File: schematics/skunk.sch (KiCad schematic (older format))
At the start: 11 parts

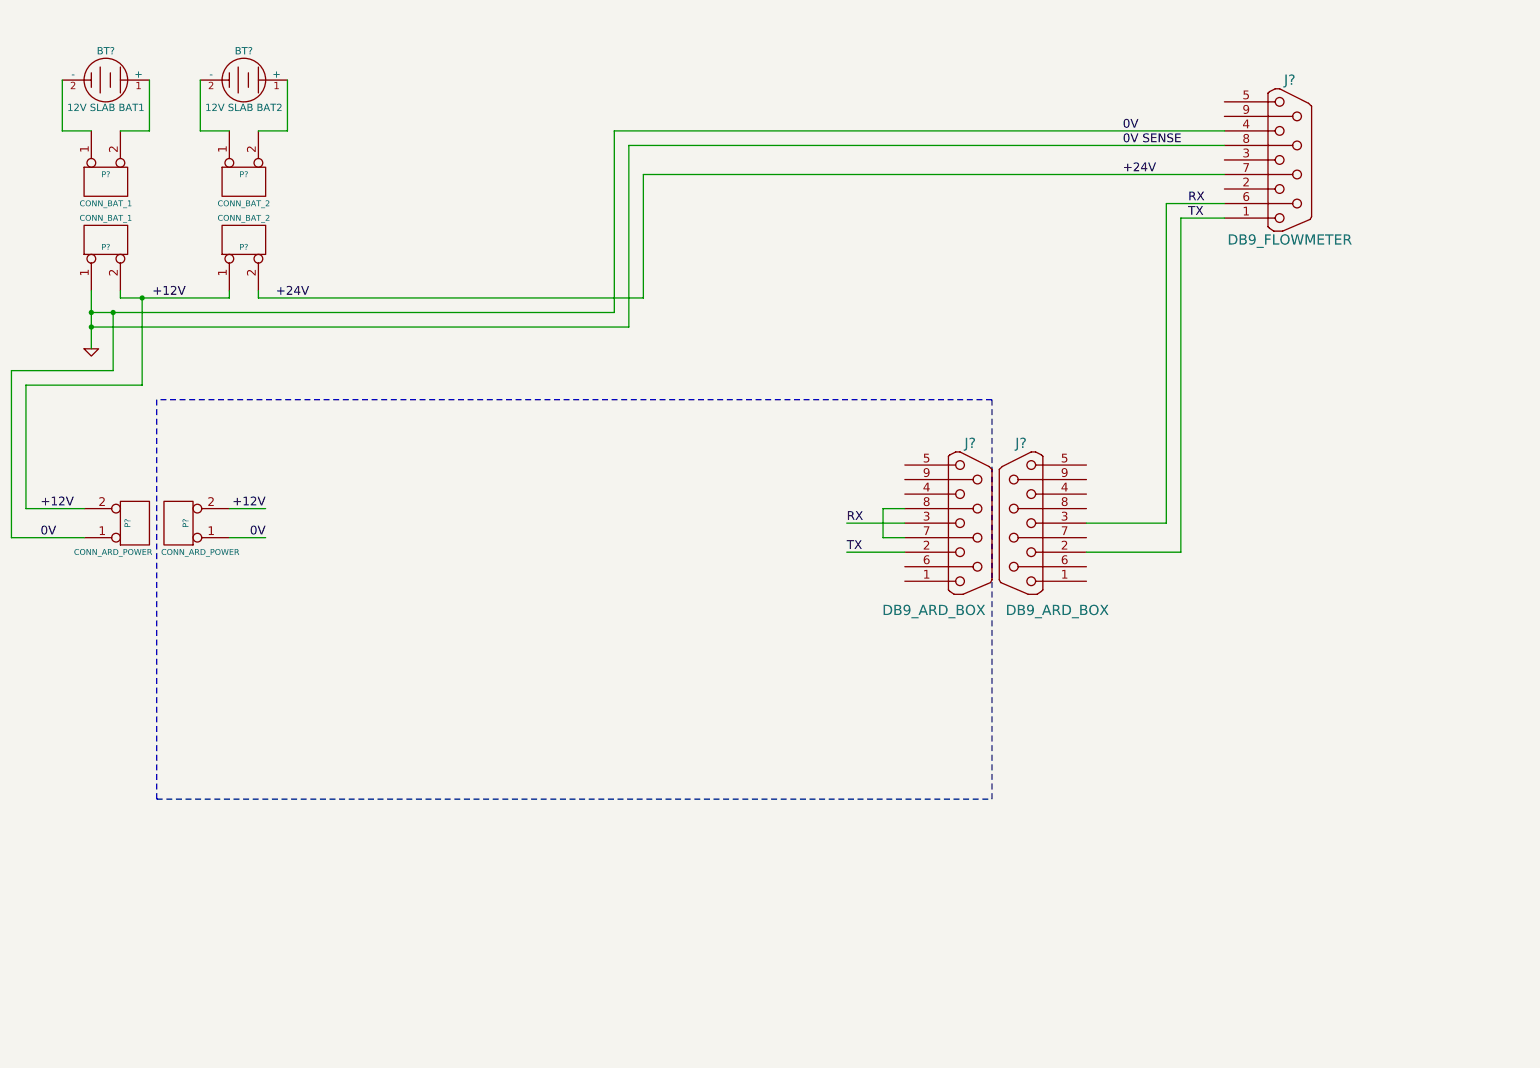
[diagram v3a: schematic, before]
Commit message: Added peripheral DB25 connectors
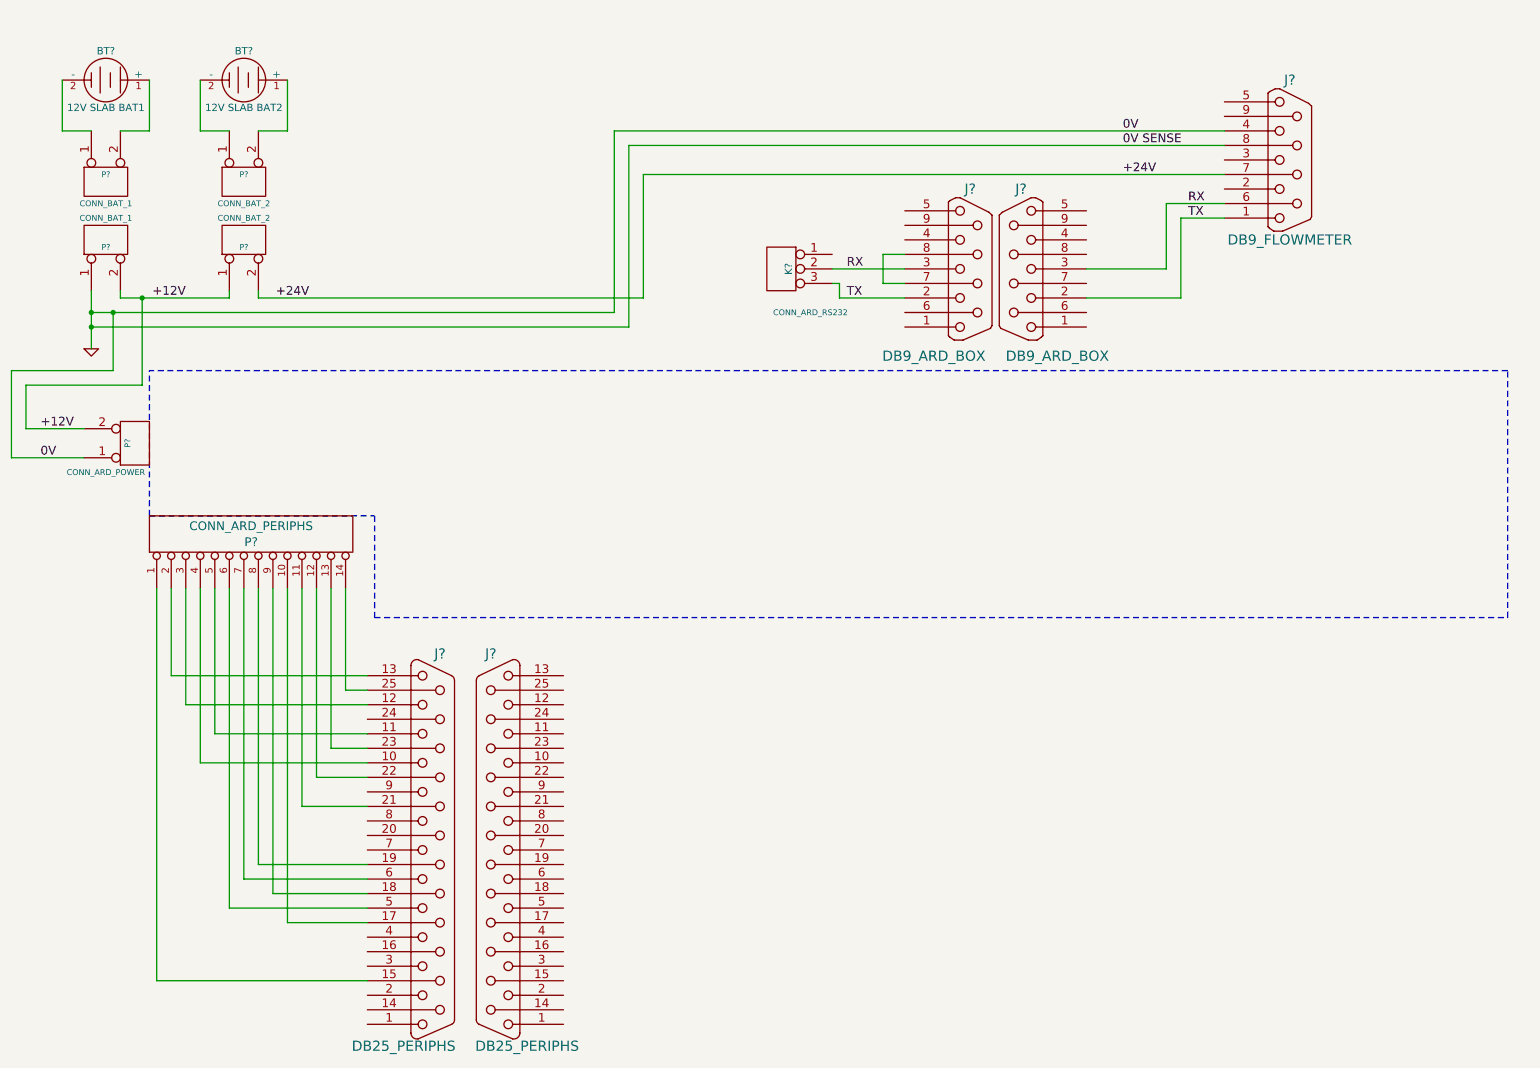
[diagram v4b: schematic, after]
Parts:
- removed P?: CONN_ARD_POWER, symbol CONN_2
- added J? (x2): DB25_PERIPHS, symbol DB25
- added K?: CONN_ARD_RS232, symbol CONN_3
- added P?: CONN_ARD_PERIPHS, symbol CONN_14
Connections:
- net RX: now also K?.2 (PM)
- net TX: now also K?.3 (P3)
- new net: J?.15 (P15), P?.1 (P1)
- new net: J?.17 (P17), P?.10 (P10)
- new net: J?.21 (P21), P?.11 (P11)
- new net: J?.22 (P22), P?.12 (P12)
- new net: J?.23 (P23), P?.13 (P13)
- new net: J?.25 (P25), P?.14 (P14)
- new net: J?.13, P?.2 (P2)
- new net: J?.12, P?.3 (P3)
- new net: J?.10, P?.4 (P4)
- new net: J?.11, P?.5 (P5)
- new net: J?.5, P?.6 (P6)
- new net: J?.6, P?.7 (P7)
- new net: J?.19 (P19), P?.8 (P8)
- new net: J?.18 (P18), P?.9 (P9)
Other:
- moved on the sheet: J?, P?
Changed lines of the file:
@@
-EESchema Schematic File Version 2  date 26/09/2012 21:43:37
+EESchema Schematic File Version 2  date 26/09/2012 22:15:26
 LIBS:power
 LIBS:device
@@
 $EndDescr
 Wire Notes Line
-	1750 5950 1750 3200
-Wire Notes Line
-	1750 5950 7500 5950
-Wire Notes Line
-	7500 5950 7500 3200
-Wire Notes Line
-	7500 3200 1750 3200
+	1700 4000 1700 3000
+Wire Wire Line
+	8150 2500 8800 2500
+Wire Wire Line
+	8800 2500 8800 1950
+Wire Wire Line
+	3200 6700 2250 6700
+Wire Wire Line
+	3200 6500 2350 6500
+Wire Wire Line
+	3200 6000 2750 6000
+Wire Wire Line
+	3200 5700 2050 5700
+Wire Wire Line
+	3200 5500 2150 5500
+Wire Wire Line
+	3200 5200 3050 5200
+Wire Wire Line
+	3200 6800 2650 6800
+Wire Wire Line
+	3050 5200 3050 4500
+Wire Wire Line
+	2850 4500 2850 5800
+Wire Wire Line
+	2650 6800 2650 4500
+Wire Wire Line
+	2450 4500 2450 6400
+Wire Wire Line
+	2250 6700 2250 4500
+Wire Wire Line
+	2050 5700 2050 4500
+Wire Wire Line
+	1850 4500 1850 5100
+Wire Wire Line
+	750  3000 750  3600
 Wire Wire Line
 	9100 1850 8700 1850
 Wire Wire Line
-	8700 1850 8700 4050
-Wire Wire Line
-	6900 4250 6500 4250
-Wire Wire Line
 	9100 1450 5000 1450
 Wire Wire Line
@@
 Wire Wire Line
 	5000 2700 1300 2700
-Wire Wire Line
-	2250 4150 2500 4150
 Connection ~ 1300 2700
 Wire Wire Line
@@
 	1450 3000 750  3000
 Wire Wire Line
-	750  3000 750  4150
-Wire Wire Line
-	8700 4050 8150 4050
-Wire Wire Line
-	1250 3950 850  3950
+	1250 3400 850  3400
 Connection ~ 1650 2500
 Wire Wire Line
@@
 Connection ~ 1300 2600
 Wire Wire Line
-	750  4150 1250 4150
+	750  3600 1250 3600
 Wire Wire Line
 	2450 2450 2450 2500
 Wire Wire Line
-	6900 3950 6750 3950
-Wire Wire Line
-	6750 3950 6750 4150
-Wire Wire Line
-	6750 4150 6900 4150
+	6900 2200 6750 2200
+Wire Wire Line
+	6750 2200 6750 2400
+Wire Wire Line
+	6750 2400 6900 2400
 Connection ~ 1450 2600
 Wire Wire Line
-	850  3950 850  3100
-Wire Wire Line
-	850  3100 1650 3100
+	1650 3100 850  3100
 Wire Wire Line
 	1650 3100 1650 2500
 Wire Wire Line
-	2500 3950 2250 3950
-Wire Wire Line
 	1300 2600 4900 2600
 Wire Wire Line
@@
 	5100 1650 9100 1650
 Wire Wire Line
-	6500 4050 6900 4050
-Wire Wire Line
-	8150 4250 8800 4250
-Wire Wire Line
-	8800 4250 8800 1950
-Wire Wire Line
 	8800 1950 9100 1950
-Text Label 6500 4050 0    60   ~ 0
+Wire Wire Line
+	6400 2300 6900 2300
+Wire Wire Line
+	6400 2400 6450 2400
+Wire Wire Line
+	6450 2400 6450 2500
+Wire Wire Line
+	6450 2500 6900 2500
+Wire Wire Line
+	850  3100 850  3400
+Wire Wire Line
+	1750 4500 1750 7200
+Wire Wire Line
+	1950 4500 1950 5300
+Wire Wire Line
+	2150 5500 2150 4500
+Wire Wire Line
+	2350 6500 2350 4500
+Wire Wire Line
+	2550 4500 2550 6600
+Wire Wire Line
+	2750 6000 2750 4500
+Wire Wire Line
+	2950 4500 2950 5600
+Wire Wire Line
+	1750 7200 3200 7200
+Wire Wire Line
+	1850 5100 3200 5100
+Wire Wire Line
+	1950 5300 3200 5300
+Wire Wire Line
+	2950 5600 3200 5600
+Wire Wire Line
+	2850 5800 3200 5800
+Wire Wire Line
+	2450 6400 3200 6400
+Wire Wire Line
+	2550 6600 3200 6600
+Wire Wire Line
+	8700 1850 8700 2300
+Wire Wire Line
+	8700 2300 8150 2300
+Wire Notes Line
+	1700 4000 3250 4000
+Wire Notes Line
+	3250 4000 3250 4700
+Wire Notes Line
+	3250 4700 11050 4700
+Wire Notes Line
+	11050 4700 11050 3000
+Wire Notes Line
+	11050 3000 1700 3000
+$Comp
+L DB25 J?
+U 1 1 50636BD9
+P 4100 6300
+F 0 "J?" H 4150 7650 70  0000 C CNN
+F 1 "DB25_PERIPHS" H 3900 4950 70  0000 C CNN
+	1    4100 6300
+	-1   0    0    -1
+$EndComp
+$Comp
+L DB25 J?
+U 1 1 50636AAF
+P 3650 6300
+F 0 "J?" H 3700 7650 70  0000 C CNN
+F 1 "DB25_PERIPHS" H 3450 4950 70  0000 C CNN
+	1    3650 6300
+	1    0    0    -1
+$EndComp
+$Comp
+L CONN_14 P?
+U 1 1 50636A9D
+P 2400 4150
+F 0 "P?" V 2370 4150 60  0000 C CNN
+F 1 "CONN_ARD_PERIPHS" V 2480 4150 60  0000 C CNN
+	1    2400 4150
+	0    -1   -1   0
+$EndComp
+$Comp
+L CONN_3 K?
+U 1 1 50636A67
+P 6050 2300
+F 0 "K?" V 6000 2300 50  0000 C CNN
+F 1 "CONN_ARD_RS232" H 5850 2000 40  0000 C CNN
+	1    6050 2300
+	-1   0    0    -1
+$EndComp
+Text Label 6500 2300 0    60   ~ 0
 RX
-Text Label 2500 4150 2    60   ~ 0
-0V
-Text Label 2500 3950 2    60   ~ 0
-+12V
 Text Label 8400 1450 0    60   ~ 0
 0V SENSE
@@
 Text Label 8400 1350 0    60   ~ 0
 0V
-Text Label 950  4150 0    60   ~ 0
+Text Label 950  3600 0    60   ~ 0
 0V
-Text Label 950  3950 0    60   ~ 0
+Text Label 950  3400 0    60   ~ 0
 +12V
 $Comp
@@
 	1    0    0    -1
 $EndComp
-Text Label 6500 4250 0    60   ~ 0
+Text Label 6500 2500 0    60   ~ 0
 TX
 $Comp
 L DB9 J?
 U 1 1 50636112
-P 7350 4050
-F 0 "J?" H 7350 4600 70  0000 C CNN
-F 1 "DB9_ARD_BOX" H 7100 3450 70  0000 C CNN
-	1    7350 4050
+P 7350 2300
+F 0 "J?" H 7350 2850 70  0000 C CNN
+F 1 "DB9_ARD_BOX" H 7100 1700 70  0000 C CNN
+	1    7350 2300
 	1    0    0    -1
 $EndComp
@@
 L DB9 J?
 U 1 1 506360FD
-P 7700 4050
-F 0 "J?" H 7700 4600 70  0000 C CNN
-F 1 "DB9_ARD_BOX" H 7450 3450 70  0000 C CNN
-	1    7700 4050
+P 7700 2300
+F 0 "J?" H 7700 2850 70  0000 C CNN
+F 1 "DB9_ARD_BOX" H 7450 1700 70  0000 C CNN
+	1    7700 2300
 	-1   0    0    -1
-$EndComp
-$Comp
-L CONN_2 P?
-U 1 1 50635EC9
-P 1900 4050
-F 0 "P?" V 1850 4050 40  0000 C CNN
-F 1 "CONN_ARD_POWER" H 1750 4250 40  0000 C CNN
-	1    1900 4050
-	-1   0    0    1
 $EndComp
 $Comp
 L CONN_2 P?
 U 1 1 50635E8C
-P 1600 4050
-F 0 "P?" V 1550 4050 40  0000 C CNN
-F 1 "CONN_ARD_POWER" H 1450 4250 40  0000 C CNN
-	1    1600 4050
+P 1600 3500
+F 0 "P?" V 1550 3500 40  0000 C CNN
+F 1 "CONN_ARD_POWER" H 1400 3700 40  0000 C CNN
+	1    1600 3500
 	1    0    0    1
 $EndComp

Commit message: Added peripherals & DB25 to schematic
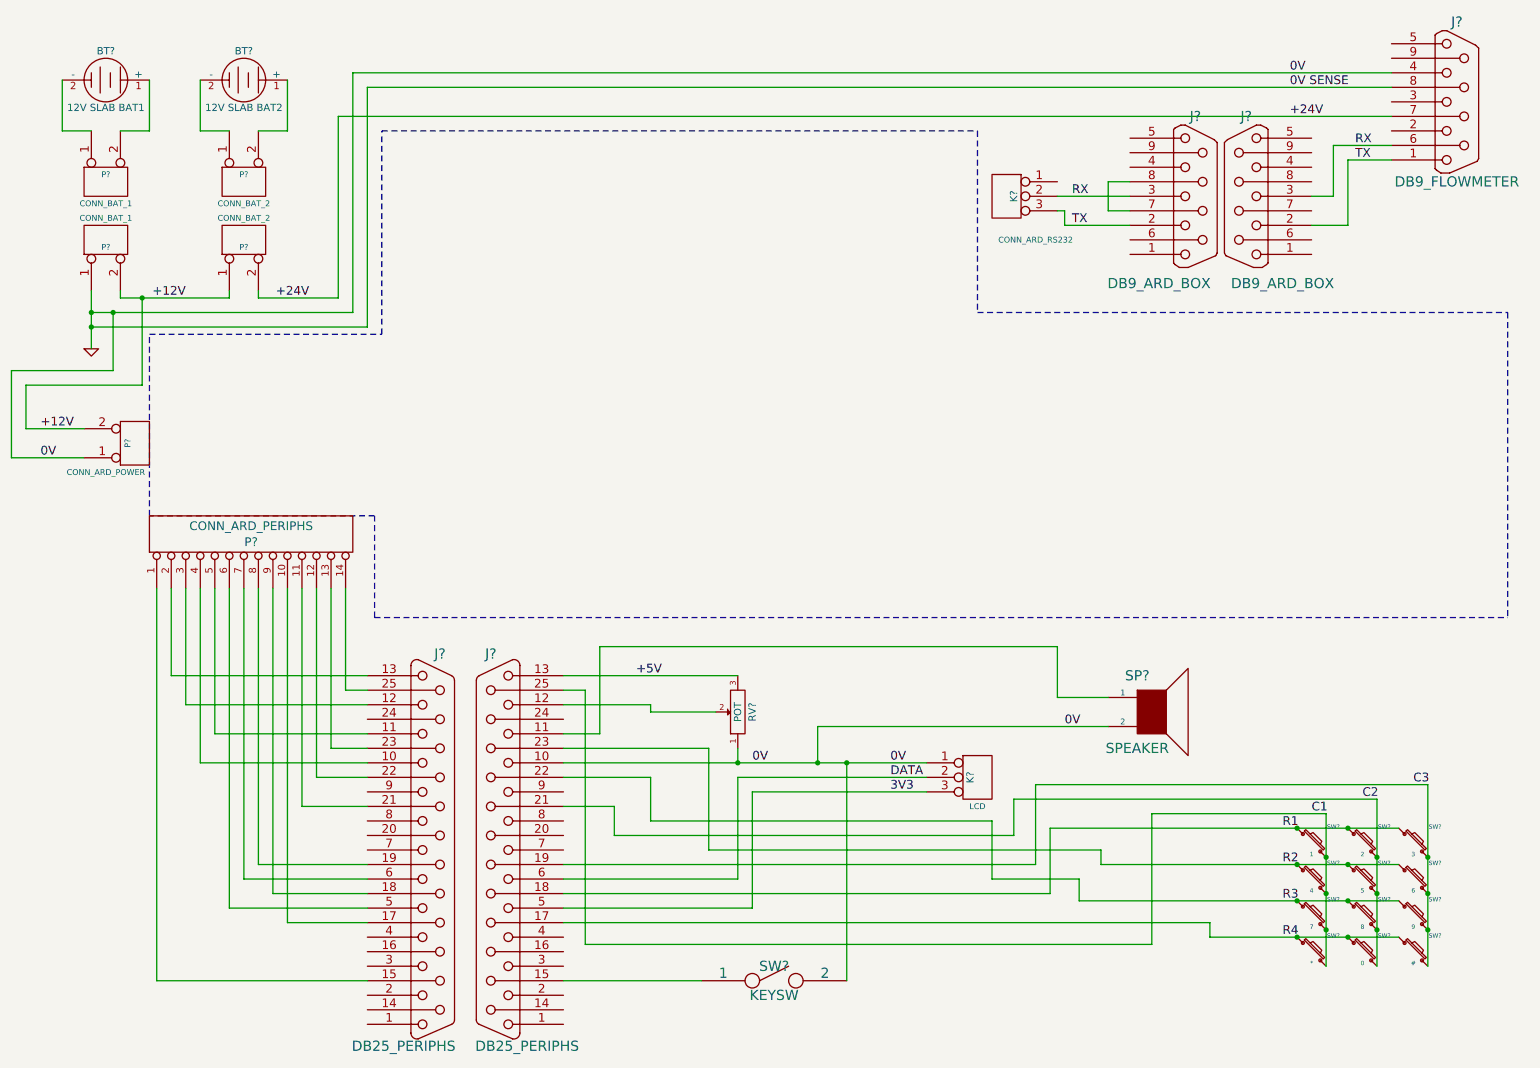
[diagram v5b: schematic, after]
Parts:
- added K?: LCD, symbol CONN_3
- added RV?: POT, symbol POT
- added SP?: SPEAKER, symbol SPEAKER
- added SW?: 1, symbol SW_PUSH_SMALL
- added SW?: 2, symbol SW_PUSH_SMALL
- added SW?: 3, symbol SW_PUSH_SMALL
- added SW?: 4, symbol SW_PUSH_SMALL
- added SW?: 5, symbol SW_PUSH_SMALL
- added SW?: 6, symbol SW_PUSH_SMALL
- added SW?: 7, symbol SW_PUSH_SMALL
- added SW?: 8, symbol SW_PUSH_SMALL
- added SW?: 9, symbol SW_PUSH_SMALL
- added SW?: *, symbol SW_PUSH_SMALL
- added SW?: 0, symbol SW_PUSH_SMALL
- added SW?: #, symbol SW_PUSH_SMALL
- added SW?: KEYSW, symbol SPST
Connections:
- net GND: now also J?.10, K?.1 (P1), RV?.1, SP?.2, SW?.2
- net at J?.11: now also SP?.1
- net at J?.12: now also RV?.2
- net +5V: now reaches J?.13
- net +5V: now also RV?.3
- net at J?.15 (P15): now also SW?.1
- net R4: now reaches J?.17 (P17)
- net R4: now also SW?.1, SW?.1, SW?.1
- net R1: now reaches J?.18 (P18)
- net R1: now also SW?.1, SW?.1, SW?.1
- net C3: now reaches J?.19 (P19)
- net C3: now also SW?.2, SW?.2, SW?.2, SW?.2
- net C2: now reaches J?.21 (P21)
- net C2: now also SW?.2, SW?.2, SW?.2, SW?.2
- net R3: now reaches J?.22 (P22)
- net R3: now also SW?.1, SW?.1, SW?.1
- net R2: now reaches J?.23 (P23)
- net R2: now also SW?.1, SW?.1, SW?.1
- net C1: now reaches J?.25 (P25)
- net C1: now also SW?.2, SW?.2, SW?.2, SW?.2
- net 3V3: now reaches J?.5
- net 3V3: now also K?.3 (P3)
- net DATA: now reaches J?.6
- net DATA: now also K?.2 (PM)
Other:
- moved on the sheet: J?, K?
